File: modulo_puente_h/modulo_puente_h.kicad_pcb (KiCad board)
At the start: 2 copper layers, 48.5 x 38 mm, 16 parts, among them J1 Conn_01x07_Pin, M1 Motor_IZQ, M2 Motor_DER, U1 L298N

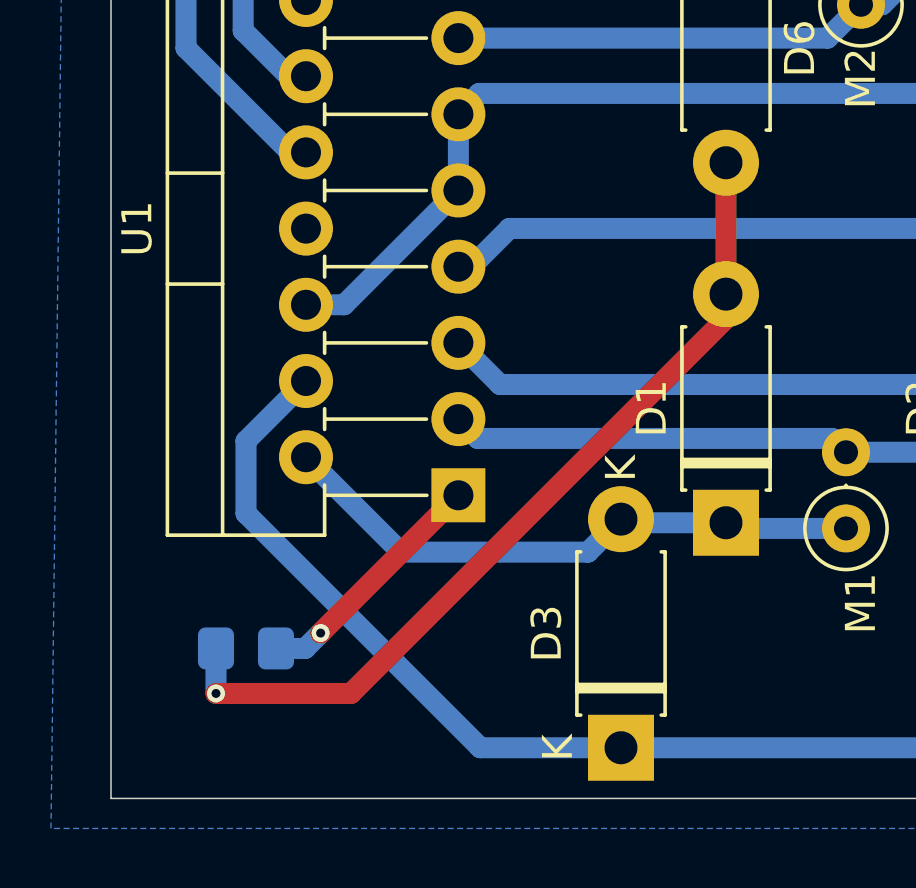
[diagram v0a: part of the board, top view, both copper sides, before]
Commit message: refactor(puente-h): Ensancho espacios entre pistas
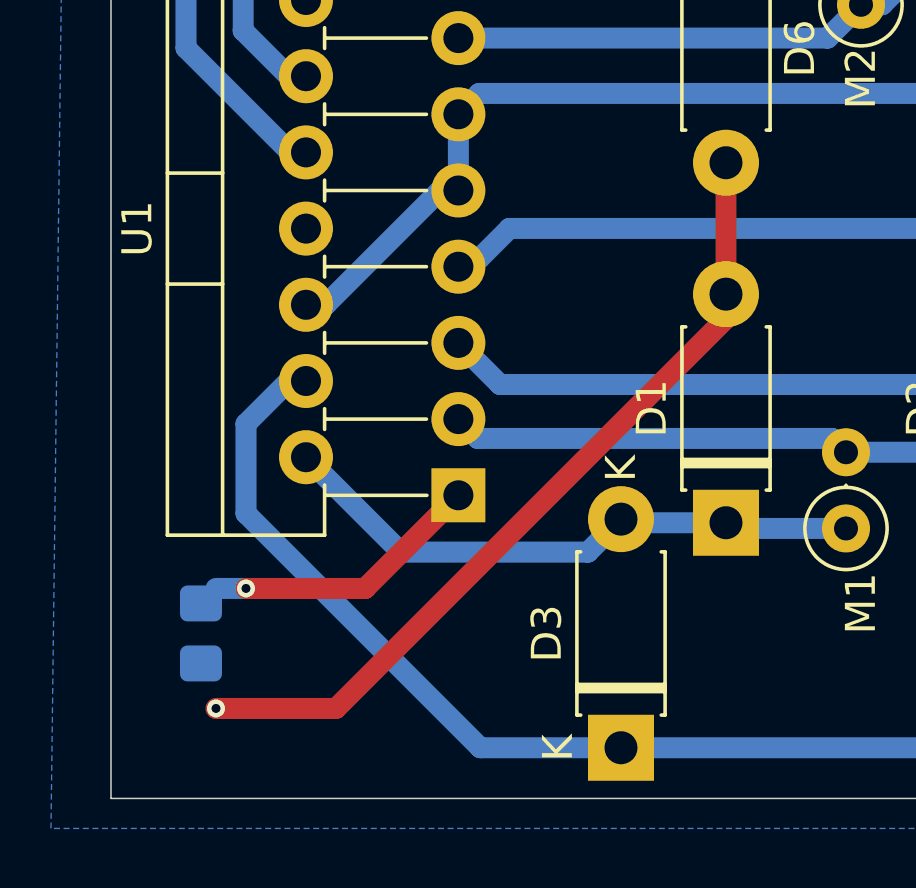
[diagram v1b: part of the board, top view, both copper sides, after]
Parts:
- moved R1 1.58 mm to (103.0, 82.5), turned to -90 degrees
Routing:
- net GND: track 35.1 -> 33.8 mm
- net Net-(U1-SENSE_A): track 8.19 -> 9.37 mm
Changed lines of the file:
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@@
 	(footprint "Resistor_SMD:R_0805_2012Metric_Pad1.20x1.40mm_HandSolder"
 		(layer "B.Cu")
-		(at 104.5 83 180)
+		(at 103 82.5 -90)
 		(descr "Resistor SMD 0805 (2012 Metric), square (rectangular) end terminal, IPC_7351 nominal with elongated pad for handsoldering. (Body size source: IPC-SM-782 page 72, https://www.pcb-3d.com/wordpress/wp-content/uploads/ipc-sm-782a_amendment_1_and_2.pdf), generated with kicad-footprint-generator")
 		(tags "resistor handsolder")
 		(property "Reference" "R1"
-			(at 0 1.65 0)
+			(at 0 1.65 90)
 			(layer "B.SilkS")
 			(effects
@@
 		)
 		(property "Value" "R_US"
-			(at 0 -1.65 0)
+			(at 0 -1.65 90)
 			(layer "B.Fab")
 			(effects
@@
 		)
 		(property "Datasheet" ""
-			(at 0 0 0)
+			(at 0 0 90)
 			(unlocked yes)
 			(layer "B.Fab")
@@
 		)
 		(property "Description" "Resistor, US symbol"
-			(at 0 0 0)
+			(at 0 0 90)
 			(unlocked yes)
 			(layer "B.Fab")
@@
 		)
 		(fp_line
+			(start -1.85 0.95)
+			(end 1.85 0.95)
+			(stroke
+				(width 0.05)
+				(type solid)
+			)
+			(layer "B.CrtYd")
+		)
+		(fp_line
 			(start 1.85 0.95)
 			(end 1.85 -0.95)
@@
 		)
 		(fp_line
+			(start -1.85 -0.95)
+			(end -1.85 0.95)
+			(stroke
+				(width 0.05)
+				(type solid)
+			)
+			(layer "B.CrtYd")
+		)
+		(fp_line
 			(start 1.85 -0.95)
 			(end -1.85 -0.95)
@@
 		)
 		(fp_line
-			(start -1.85 0.95)
-			(end 1.85 0.95)
-			(stroke
-				(width 0.05)
-				(type solid)
-			)
-			(layer "B.CrtYd")
-		)
-		(fp_line
-			(start -1.85 -0.95)
-			(end -1.85 0.95)
-			(stroke
-				(width 0.05)
-				(type solid)
-			)
-			(layer "B.CrtYd")
+			(start -1 0.625)
+			(end 1 0.625)
+			(stroke
+				(width 0.1)
+				(type solid)
+			)
+			(layer "B.Fab")
 		)
 		(fp_line
@@
 		)
 		(fp_line
+			(start -1 -0.625)
+			(end -1 0.625)
+			(stroke
+				(width 0.1)
+				(type solid)
+			)
+			(layer "B.Fab")
+		)
+		(fp_line
 			(start 1 -0.625)
 			(end -1 -0.625)
@@
 			(layer "B.Fab")
 		)
-		(fp_line
-			(start -1 0.625)
-			(end 1 0.625)
-			(stroke
-				(width 0.1)
-				(type solid)
-			)
-			(layer "B.Fab")
-		)
-		(fp_line
-			(start -1 -0.625)
-			(end -1 0.625)
-			(stroke
-				(width 0.1)
-				(type solid)
-			)
-			(layer "B.Fab")
-		)
 		(fp_text user "${REFERENCE}"
-			(at 0 0 0)
+			(at 0 0 90)
 			(layer "B.Fab")
 			(effects
@@
 		)
 		(pad "1" smd roundrect
-			(at -1 0 180)
+			(at -1 0 270)
 			(size 1.2 1.4)
 			(layers "B.Cu" "B.Mask" "B.Paste")
@@
 		)
 		(pad "2" smd roundrect
-			(at 1 0 180)
+			(at 1 0 270)
 			(size 1.2 1.4)
 			(layers "B.Cu" "B.Mask" "B.Paste")
@@
 	)
 	(segment
-		(start 103.5 84.5)
-		(end 108 84.5)
+		(start 107.5 85)
+		(end 120.5 72)
 		(width 0.7)
 		(layer "F.Cu")
@@
 	)
 	(segment
+		(start 103.5 85)
+		(end 107.5 85)
+		(width 0.7)
+		(layer "F.Cu")
+		(net 1)
+	)
+	(segment
 		(start 144.08 76.08)
 		(end 140 72)
@@
 	)
 	(segment
-		(start 108 84.5)
-		(end 120.5 72)
+		(start 120.5 72)
+		(end 120.5 71.19)
 		(width 0.7)
 		(layer "F.Cu")
 		(net 1)
 	)
-	(segment
-		(start 120.5 72)
-		(end 120.5 71.19)
-		(width 0.7)
-		(layer "F.Cu")
-		(net 1)
-	)
 	(via
-		(at 103.5 84.5)
+		(at 103.5 85)
 		(size 0.6)
 		(drill 0.3)
@@
 	)
 	(segment
-		(start 103.5 83)
-		(end 103.5 84.5)
-		(width 0.7)
-		(layer "B.Cu")
-		(net 1)
+		(start 104.5 75.513122)
+		(end 104.5 78.5)
+		(width 0.7)
+		(layer "B.Cu")
+		(net 2)
 	)
 	(segment
@@
 	)
 	(segment
-		(start 106.5 74.085)
-		(end 104.5 76.085)
-		(width 0.7)
-		(layer "B.Cu")
-		(net 2)
-	)
-	(segment
 		(start 143.5 82.5)
 		(end 139.69 86.31)
@@
 	)
 	(segment
-		(start 104.5 76.085)
-		(end 104.5 78.5)
+		(start 104.5 78.5)
+		(end 112.31 86.31)
 		(width 0.7)
 		(layer "B.Cu")
@@
 	)
 	(segment
-		(start 104.5 78.5)
-		(end 112.31 86.31)
+		(start 105.928122 74.085)
+		(end 104.5 75.513122)
 		(width 0.7)
 		(layer "B.Cu")
@@
 	)
 	(segment
+		(start 106.5 74.085)
+		(end 105.928122 74.085)
+		(width 0.7)
+		(layer "B.Cu")
+		(net 2)
+	)
+	(segment
 		(start 135.19 51.69)
 		(end 144.34 60.84)
@@
 	)
 	(segment
+		(start 106.5 71.545)
+		(end 107.15875 71.545)
+		(width 0.7)
+		(layer "B.Cu")
+		(net 3)
+	)
+	(segment
 		(start 140.5 67.5)
 		(end 137.5 64.5)
@@
 	)
 	(segment
-		(start 107.77 71.545)
+		(start 110.96875 67.735)
 		(end 111.58 67.735)
 		(width 0.7)
@@
 	)
 	(segment
+		(start 107.15875 71.545)
+		(end 110.96875 67.735)
+		(width 0.7)
+		(layer "B.Cu")
+		(net 3)
+	)
+	(segment
 		(start 111.58 67.735)
 		(end 111.58 65.195)
@@
 	)
 	(segment
-		(start 106.5 71.545)
-		(end 107.77 71.545)
-		(width 0.7)
-		(layer "B.Cu")
-		(net 3)
-	)
-	(segment
 		(start 144.46 68.5)
 		(end 144.5 68.46)
@@
 	)
 	(segment
+		(start 111.58 75.355)
+		(end 112.225 76)
+		(width 0.7)
+		(layer "B.Cu")
+		(net 5)
+	)
+	(segment
+		(start 124.04 76)
+		(end 124.5 76.46)
+		(width 0.7)
+		(layer "B.Cu")
+		(net 5)
+	)
+	(segment
 		(start 127.15 76.46)
 		(end 129.5 78.81)
@@
 	)
 	(segment
-		(start 111.58 75.355)
-		(end 112.225 76)
-		(width 0.7)
-		(layer "B.Cu")
-		(net 5)
-	)
-	(segment
 		(start 124.5 76.46)
 		(end 127.15 76.46)
@@
 	)
 	(segment
-		(start 124.04 76)
-		(end 124.5 76.46)
-		(width 0.7)
-		(layer "B.Cu")
-		(net 5)
-	)
-	(segment
 		(start 129.5 59.19)
 		(end 132.88 59.19)
@@
 	)
 	(segment
+		(start 128.06 59.19)
+		(end 129.5 59.19)
+		(width 0.7)
+		(layer "B.Cu")
+		(net 6)
+	)
+	(segment
+		(start 132.88 59.19)
+		(end 133 59.31)
+		(width 0.7)
+		(layer "B.Cu")
+		(net 6)
+	)
+	(segment
+		(start 111.58 62.655)
+		(end 123.89 62.655)
+		(width 0.7)
+		(layer "B.Cu")
+		(net 6)
+	)
+	(segment
 		(start 125 61.545)
 		(end 125.705 61.545)
@@
 	)
 	(segment
-		(start 128.06 59.19)
-		(end 129.5 59.19)
-		(width 0.7)
-		(layer "B.Cu")
-		(net 6)
-	)
-	(segment
 		(start 125.705 61.545)
 		(end 128.06 59.19)
@@
 	)
 	(segment
-		(start 132.88 59.19)
-		(end 133 59.31)
-		(width 0.7)
-		(layer "B.Cu")
-		(net 6)
-	)
-	(segment
-		(start 111.58 62.655)
-		(end 123.89 62.655)
-		(width 0.7)
-		(layer "B.Cu")
-		(net 6)
-	)
-	(segment
 		(start 124.815 59.19)
 		(end 125 59.005)
@@
 	)
 	(segment
-		(start 106.9875 82.4875)
-		(end 111.58 77.895)
+		(start 104.5 81)
+		(end 108.475 81)
 		(width 0.7)
 		(layer "F.Cu")
 		(net 12)
 	)
+	(segment
+		(start 108.475 81)
+		(end 111.58 77.895)
+		(width 0.7)
+		(layer "F.Cu")
+		(net 12)
+	)
 	(via
-		(at 106.9875 82.4875)
+		(at 104.5 81)
 		(size 0.6)
 		(drill 0.3)
@@
 	)
 	(segment
-		(start 106.475 83)
-		(end 106.9875 82.4875)
-		(width 0.7)
-		(layer "B.Cu")
-		(net 12)
-	)
-	(segment
-		(start 105.5 83)
-		(end 106.475 83)
+		(start 104.5 81)
+		(end 103.5 81)
 		(width 0.7)
 		(layer "B.Cu")
@@
 		(min_thickness 0.25)
 		(filled_areas_thickness no)
-		(fill yes
+		(fill
 			(thermal_gap 0.5)
 			(thermal_bridge_width 0.5)
